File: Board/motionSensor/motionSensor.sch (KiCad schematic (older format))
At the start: 15 parts, among them J1 SWD CONNECTOR, SW1 SW_Push, U1 MKL25Z128VLK4

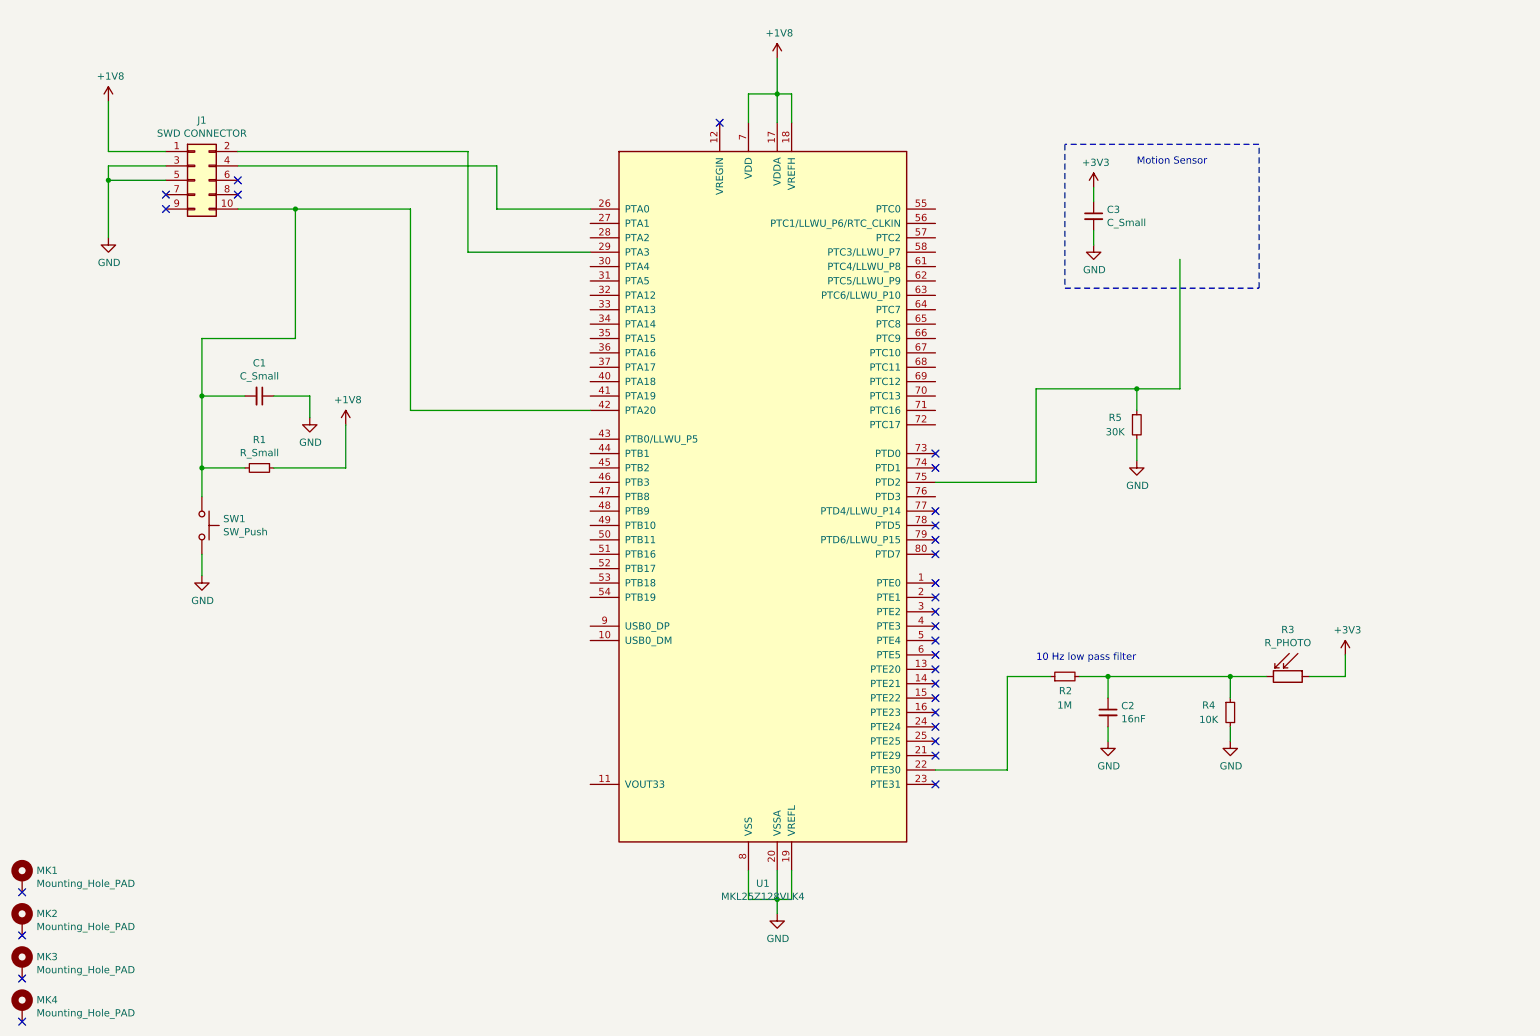
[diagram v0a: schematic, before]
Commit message: Add power supply, crystal, LED strip and motion sensor
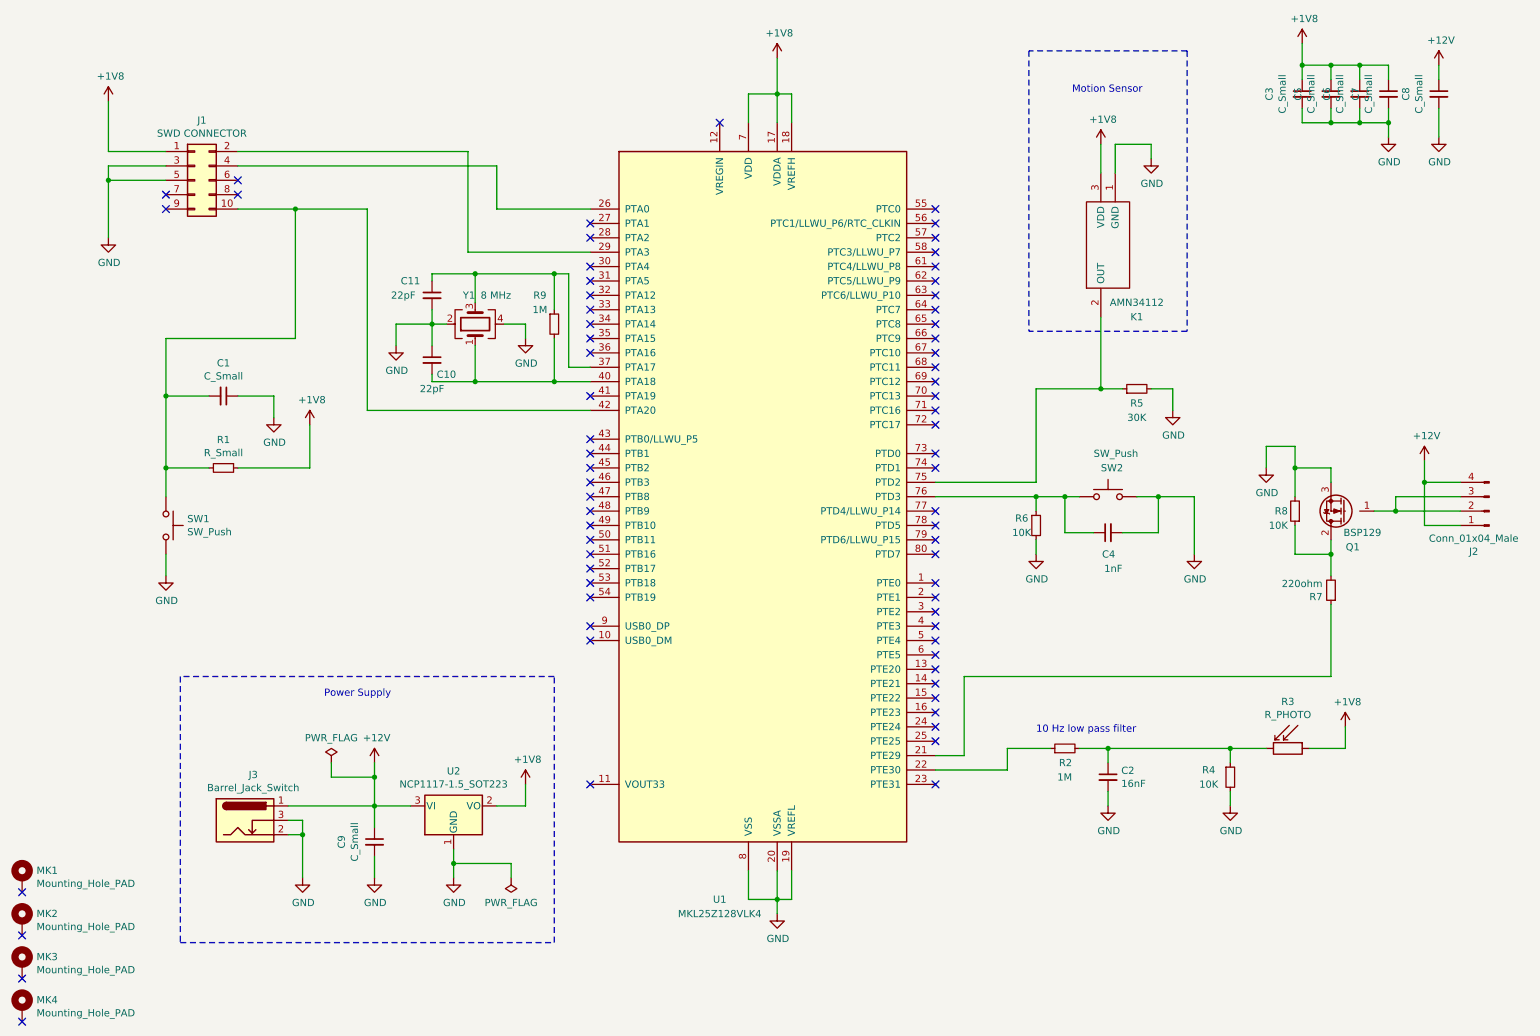
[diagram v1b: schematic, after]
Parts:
- added C10, C11: 22pF, symbol Device:C_Small
- added C4: 1nF, symbol Device:C_Small
- added C5, C6, C7, C8, C9: C_Small, symbol Device:C_Small
- added J2: Conn_01x04_Male, symbol Connector:Conn_01x04_Male
- added J3: Barrel_Jack_Switch, symbol Connector:Barrel_Jack_Switch
- added K1: AMN34112, AMN34112, symbol AMN34112:AMN34112
- added Q1: BSP129, Package_TO_SOT_SMD:SOT-223-3_TabPin2, symbol Transistor_FET:BSP129
- added R6, R8: 10K, symbol Device:R_Small
- added R7: 220ohm, symbol Device:R_Small
- added R9: 1M, symbol Device:R_Small
- added SW2: SW_Push, symbol Switch:SW_Push
- added U2: NCP1117-1.5_SOT223, Package_TO_SOT_SMD:SOT-223-3_TabPin2, symbol Regulator_Linear:NCP1117-1.5_SOT223
- added Y1: 8 MHz, symbol Device:Crystal_GND24
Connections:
- net +3V3 is gone; now on net +1V8: C3.1, R3.1
- net +1V8: now also C5.1, C6.1, C7.1, K1.3 (VDD), U2.2 (VO)
- net GND: now also C10.1, C11.2, C4.2, C5.2, C6.2, C7.2, C8.2, C9.2, J3.2, J3.3, K1.1 (GND), Q1.3 (S), R6.2, R8.2, SW2.2, U2.1 (GND), Y1.2, Y1.4
- net at U1.21 (PTE29): now also R7.1
- net at U1.37 (PTA17): now also C11.1, R9.1, Y1.3
- net at U1.40 (PTA18): now also C10.2, R9.2, Y1.1
- net at R5.1, U1.75 (PTD2): now also K1.2 (OUT)
- net at U1.76 (PTD3): now also C4.1, R6.1, SW2.1
- new net: J2.2 (Pin_2), J2.3 (Pin_3), Q1.1 (G)
- new net: Q1.2 (D), R7.2, R8.1
- new net +12V: C8.1, C9.1, J2.1 (Pin_1), J2.4 (Pin_4), J3.1, U2.3 (VI)
- no-connect marks 29 -> 69
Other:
- note added: "Power Supply"
- moved on the sheet: C1, C2, R1, R2, R3, R4, R5, SW1
